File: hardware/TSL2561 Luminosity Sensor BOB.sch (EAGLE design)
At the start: 15 parts, among them U1 TSL2561FN

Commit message: Review for reds (hardware only)
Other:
- note added: "1.0"
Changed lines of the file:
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@@
 <grid distance="0.1" unitdist="inch" unit="inch" style="lines" multiple="1" display="no" altdistance="0.01" altunitdist="inch" altunit="inch"/>
 <layers>
-<layer number="1" name="Top" color="4" fill="1" visible="yes" active="no"/>
-<layer number="2" name="Route2" color="1" fill="3" visible="yes" active="no"/>
-<layer number="3" name="Route3" color="4" fill="3" visible="yes" active="no"/>
-<layer number="4" name="Route4" color="1" fill="4" visible="yes" active="no"/>
-<layer number="5" name="Route5" color="4" fill="4" visible="yes" active="no"/>
-<layer number="6" name="Route6" color="1" fill="8" visible="yes" active="no"/>
-<layer number="7" name="Route7" color="4" fill="8" visible="yes" active="no"/>
-<layer number="8" name="Route8" color="1" fill="2" visible="yes" active="no"/>
-<layer number="9" name="Route9" color="4" fill="2" visible="yes" active="no"/>
-<layer number="10" name="Route10" color="1" fill="7" visible="yes" active="no"/>
-<layer number="11" name="Route11" color="4" fill="7" visible="yes" active="no"/>
-<layer number="12" name="Route12" color="1" fill="5" visible="yes" active="no"/>
-<layer number="13" name="Route13" color="4" fill="5" visible="yes" active="no"/>
-<layer number="14" name="Route14" color="1" fill="6" visible="yes" active="no"/>
-<layer number="15" name="Route15" color="4" fill="6" visible="yes" active="no"/>
-<layer number="16" name="Bottom" color="1" fill="1" visible="yes" active="no"/>
-<layer number="17" name="Pads" color="2" fill="1" visible="yes" active="no"/>
-<layer number="18" name="Vias" color="2" fill="1" visible="yes" active="no"/>
-<layer number="19" name="Unrouted" color="6" fill="1" visible="yes" active="no"/>
-<layer number="20" name="Dimension" color="15" fill="1" visible="yes" active="no"/>
-<layer number="21" name="tPlace" color="7" fill="1" visible="yes" active="no"/>
-<layer number="22" name="bPlace" color="7" fill="1" visible="yes" active="no"/>
-<layer number="23" name="tOrigins" color="15" fill="1" visible="yes" active="no"/>
-<layer number="24" name="bOrigins" color="15" fill="1" visible="yes" active="no"/>
-<layer number="25" name="tNames" color="7" fill="1" visible="yes" active="no"/>
-<layer number="26" name="bNames" color="7" fill="1" visible="yes" active="no"/>
-<layer number="27" name="tValues" color="7" fill="1" visible="yes" active="no"/>
-<layer number="28" name="bValues" color="7" fill="1" visible="yes" active="no"/>
+<layer number="1" name="Top" color="4" fill="1" visible="no" active="no"/>
+<layer number="2" name="Route2" color="1" fill="3" visible="no" active="no"/>
+<layer number="3" name="Route3" color="4" fill="3" visible="no" active="no"/>
+<layer number="4" name="Route4" color="1" fill="4" visible="no" active="no"/>
+<layer number="5" name="Route5" color="4" fill="4" visible="no" active="no"/>
+<layer number="6" name="Route6" color="1" fill="8" visible="no" active="no"/>
+<layer number="7" name="Route7" color="4" fill="8" visible="no" active="no"/>
+<layer number="8" name="Route8" color="1" fill="2" visible="no" active="no"/>
+<layer number="9" name="Route9" color="4" fill="2" visible="no" active="no"/>
+<layer number="10" name="Route10" color="1" fill="7" visible="no" active="no"/>
+<layer number="11" name="Route11" color="4" fill="7" visible="no" active="no"/>
+<layer number="12" name="Route12" color="1" fill="5" visible="no" active="no"/>
+<layer number="13" name="Route13" color="4" fill="5" visible="no" active="no"/>
+<layer number="14" name="Route14" color="1" fill="6" visible="no" active="no"/>
+<layer number="15" name="Route15" color="4" fill="6" visible="no" active="no"/>
+<layer number="16" name="Bottom" color="1" fill="1" visible="no" active="no"/>
+<layer number="17" name="Pads" color="2" fill="1" visible="no" active="no"/>
+<layer number="18" name="Vias" color="2" fill="1" visible="no" active="no"/>
+<layer number="19" name="Unrouted" color="6" fill="1" visible="no" active="no"/>
+<layer number="20" name="Dimension" color="15" fill="1" visible="no" active="no"/>
+<layer number="21" name="tPlace" color="7" fill="1" visible="no" active="no"/>
+<layer number="22" name="bPlace" color="7" fill="1" visible="no" active="no"/>
+<layer number="23" name="tOrigins" color="15" fill="1" visible="no" active="no"/>
+<layer number="24" name="bOrigins" color="15" fill="1" visible="no" active="no"/>
+<layer number="25" name="tNames" color="7" fill="1" visible="no" active="no"/>
+<layer number="26" name="bNames" color="7" fill="1" visible="no" active="no"/>
+<layer number="27" name="tValues" color="7" fill="1" visible="no" active="no"/>
+<layer number="28" name="bValues" color="7" fill="1" visible="no" active="no"/>
 <layer number="29" name="tStop" color="7" fill="3" visible="no" active="no"/>
 <layer number="30" name="bStop" color="7" fill="6" visible="no" active="no"/>
@@
 <layer number="35" name="tGlue" color="7" fill="4" visible="no" active="no"/>
 <layer number="36" name="bGlue" color="7" fill="5" visible="no" active="no"/>
-<layer number="37" name="tTest" color="7" fill="1" visible="yes" active="no"/>
-<layer number="38" name="bTest" color="7" fill="1" visible="yes" active="no"/>
+<layer number="37" name="tTest" color="7" fill="1" visible="no" active="no"/>
+<layer number="38" name="bTest" color="7" fill="1" visible="no" active="no"/>
 <layer number="39" name="tKeepout" color="4" fill="11" visible="no" active="no"/>
 <layer number="40" name="bKeepout" color="1" fill="11" visible="no" active="no"/>
@@
 <layer number="44" name="Drills" color="7" fill="1" visible="no" active="no"/>
 <layer number="45" name="Holes" color="7" fill="1" visible="no" active="no"/>
-<layer number="46" name="Milling" color="3" fill="1" visible="yes" active="no"/>
-<layer number="47" name="Measures" color="7" fill="1" visible="yes" active="no"/>
-<layer number="48" name="Document" color="7" fill="1" visible="yes" active="no"/>
-<layer number="49" name="Reference" color="7" fill="1" visible="yes" active="no"/>
-<layer number="50" name="dxf" color="7" fill="1" visible="yes" active="no"/>
-<layer number="51" name="tDocu" color="7" fill="1" visible="yes" active="no"/>
-<layer number="52" name="bDocu" color="7" fill="1" visible="yes" active="no"/>
-<layer number="53" name="tGND_GNDA" color="7" fill="9" visible="yes" active="no"/>
-<layer number="54" name="bGND_GNDA" color="1" fill="9" visible="yes" active="no"/>
-<layer number="56" name="wert" color="7" fill="1" visible="yes" active="no"/>
+<layer number="46" name="Milling" color="3" fill="1" visible="no" active="no"/>
+<layer number="47" name="Measures" color="7" fill="1" visible="no" active="no"/>
+<layer number="48" name="Document" color="7" fill="1" visible="no" active="no"/>
+<layer number="49" name="Reference" color="7" fill="1" visible="no" active="no"/>
+<layer number="50" name="dxf" color="7" fill="1" visible="no" active="no"/>
+<layer number="51" name="tDocu" color="7" fill="1" visible="no" active="no"/>
+<layer number="52" name="bDocu" color="7" fill="1" visible="no" active="no"/>
+<layer number="53" name="tGND_GNDA" color="7" fill="9" visible="no" active="no"/>
+<layer number="54" name="bGND_GNDA" color="1" fill="9" visible="no" active="no"/>
+<layer number="56" name="wert" color="7" fill="1" visible="no" active="no"/>
 <layer number="91" name="Nets" color="2" fill="1" visible="yes" active="yes"/>
 <layer number="92" name="Busses" color="1" fill="1" visible="yes" active="yes"/>
@@
 <text x="48.26" y="132.08" size="1.778" layer="97">OPEN BOTH SIDES OF SJ1
 TO DISABLE I2C PULLUPS</text>
+<text x="239.268" y="6.604" size="2.54" layer="94" ratio="15">1.0</text>
 </plain>
 <instances>

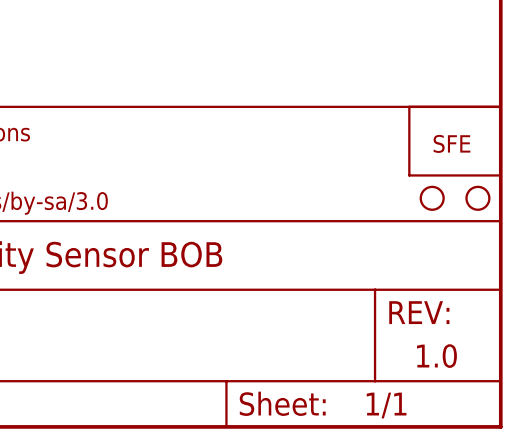
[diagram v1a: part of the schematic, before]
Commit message: Hardware version 1.0
added micro-fiducials
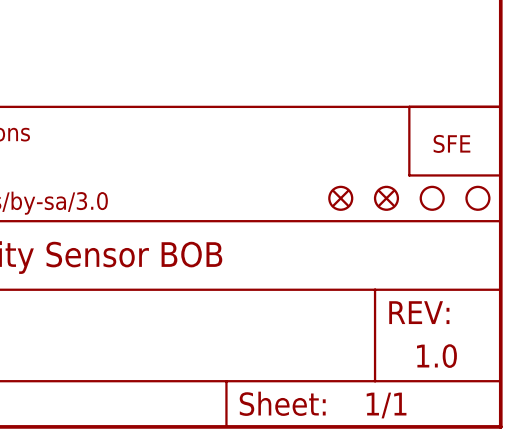
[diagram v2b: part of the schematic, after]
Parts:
- added FID1, FID2: FIDUCIALUFIDUCIAL, SparkFun-Aesthetics:FIDUCIALUFIDUCIAL
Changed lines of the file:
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@@
 <part name="R4" library="SparkFun-Resistors" deviceset="RESISTOR" device="0603" value="10K"/>
 <part name="SUPPLY5" library="SparkFun-Aesthetics" deviceset="VCC" device="" value="3.3V"/>
+<part name="FID1" library="SparkFun-Aesthetics" deviceset="FIDUCIAL" device="UFIDUCIAL"/>
+<part name="FID2" library="SparkFun-Aesthetics" deviceset="FIDUCIAL" device="UFIDUCIAL"/>
 </parts>
 <sheets>
@@
 <text x="48.26" y="132.08" size="1.778" layer="97">OPEN BOTH SIDES OF SJ1
 TO DISABLE I2C PULLUPS</text>
-<text x="239.268" y="6.604" size="2.54" layer="94" ratio="15">1.0</text>
+<text x="239.268" y="6.604" size="2.54" layer="94" ratio="10">1.0</text>
 </plain>
 <instances>
@@
 <instance part="R4" gate="G$1" x="114.3" y="124.46" rot="R90"/>
 <instance part="SUPPLY5" gate="1" x="114.3" y="142.24"/>
+<instance part="FID1" gate="G$1" x="236.22" y="25.4"/>
+<instance part="FID2" gate="G$1" x="231.14" y="25.4"/>
 </instances>
 <busses>

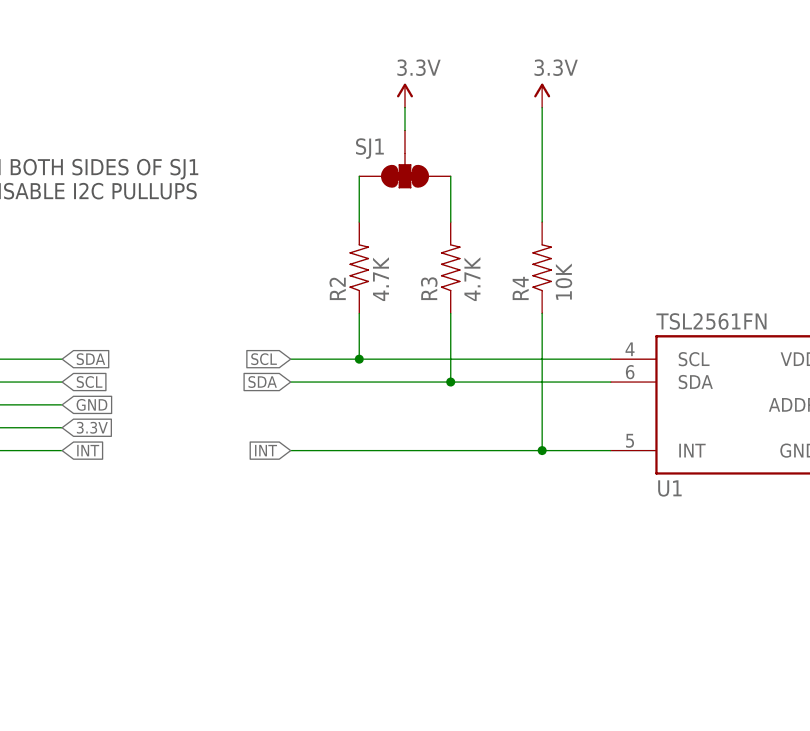
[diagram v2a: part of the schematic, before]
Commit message: Updating BRD/SCH files to current lib parts
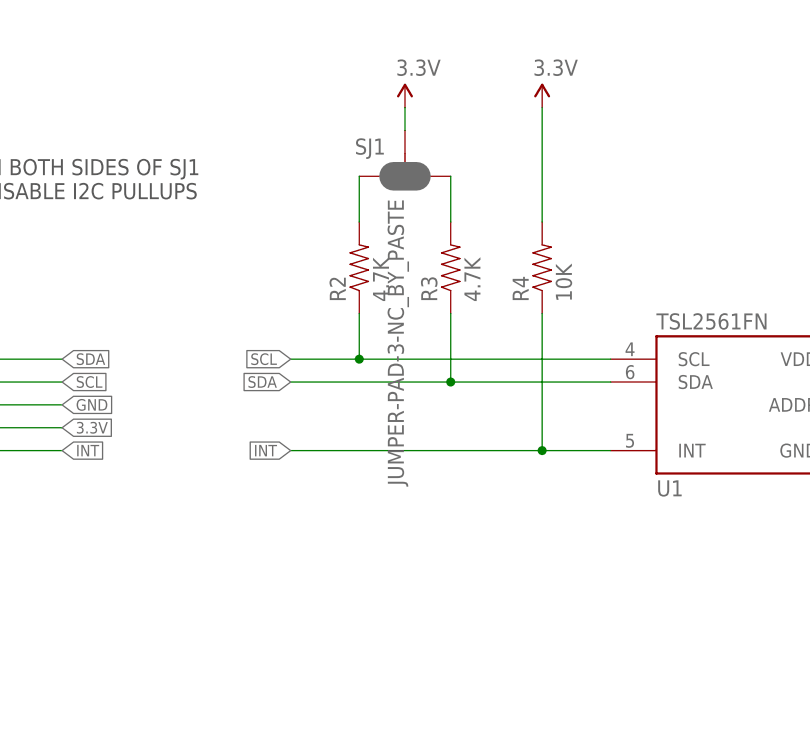
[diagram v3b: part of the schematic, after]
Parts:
- C1: device SparkFun-Capacitors:CAP0603-CAP -> SparkFun-Capacitors:0.1UF-25V(+80/-20%)(0603)
- JP1: device mike-temp:M05_ROUNDONLY_NOSILK -> SparkFun-Connectors:M05NO_SILK
- R1, R4: device SparkFun-Resistors:RESISTOR0603 -> SparkFun-Resistors:10KOHM-1/10W-1%(0603)0603
- R2, R3: device SparkFun-Resistors:RESISTOR0603 -> SparkFun-Resistors:4.7KOHM-1/10W-1%(0603)
- SJ1: value (none) -> JUMPER-PAD-3-NC_BY_PASTE; device mike-temp:SOLDERJUMPER_2WAYPASTE1&2&3 -> SparkFun-Passives:JUMPER-PAD-3-NC_BY_PASTE
- U1: device mike-temp:TSL2561FN -> SparkFun-DigitalIC:TSL2561FN
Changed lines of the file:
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@@
 <?xml version="1.0" encoding="utf-8"?>
 <!DOCTYPE eagle SYSTEM "eagle.dtd">
-<eagle version="6.4">
+<eagle version="7.2.0">
 <drawing>
 <settings>
@@
 <layer number="54" name="bGND_GNDA" color="1" fill="9" visible="no" active="no"/>
 <layer number="56" name="wert" color="7" fill="1" visible="no" active="no"/>
+<layer number="57" name="tCAD" color="7" fill="1" visible="no" active="no"/>
+<layer number="59" name="tCarbon" color="7" fill="1" visible="no" active="no"/>
+<layer number="60" name="bCarbon" color="7" fill="1" visible="no" active="no"/>
+<layer number="90" name="Modules" color="5" fill="1" visible="yes" active="yes"/>
 <layer number="91" name="Nets" color="2" fill="1" visible="yes" active="yes"/>
 <layer number="92" name="Busses" color="1" fill="1" visible="yes" active="yes"/>
@@
 <layer number="97" name="Info" color="7" fill="1" visible="yes" active="yes"/>
 <layer number="98" name="Guide" color="6" fill="1" visible="yes" active="yes"/>
+<layer number="99" name="SpiceOrder" color="7" fill="1" visible="yes" active="yes"/>
 <layer number="100" name="Muster" color="7" fill="1" visible="no" active="no"/>
 <layer number="101" name="Patch_Top" color="12" fill="4" visible="no" active="yes"/>
@@
 <layer number="108" name="tplace-old" color="10" fill="1" visible="yes" active="yes"/>
 <layer number="109" name="ref-old" color="11" fill="1" visible="yes" active="yes"/>
+<layer number="110" name="fp0" color="7" fill="1" visible="yes" active="yes"/>
+<layer number="111" name="LPC17xx" color="7" fill="1" visible="yes" active="yes"/>
+<layer number="112" name="tSilk" color="7" fill="1" visible="yes" active="yes"/>
+<layer number="113" name="IDFDebug" color="7" fill="1" visible="yes" active="yes"/>
 <layer number="116" name="Patch_BOT" color="9" fill="4" visible="no" active="yes"/>
 <layer number="121" name="_tsilk" color="7" fill="1" visible="no" active="yes"/>
 <layer number="122" name="_bsilk" color="7" fill="1" visible="no" active="yes"/>
+<layer number="123" name="tTestmark" color="7" fill="1" visible="yes" active="yes"/>
+<layer number="124" name="bTestmark" color="7" fill="1" visible="yes" active="yes"/>
 <layer number="125" name="_tNames" color="7" fill="1" visible="no" active="yes"/>
+<layer number="126" name="_bNames" color="7" fill="1" visible="yes" active="yes"/>
+<layer number="127" name="_tValues" color="7" fill="1" visible="yes" active="yes"/>
+<layer number="128" name="_bValues" color="7" fill="1" visible="yes" active="yes"/>
+<layer number="129" name="Mask" color="7" fill="1" visible="yes" active="yes"/>
+<layer number="131" name="tAdjust" color="7" fill="1" visible="yes" active="yes"/>
+<layer number="132" name="bAdjust" color="7" fill="1" visible="yes" active="yes"/>
 <layer number="144" name="Drill_legend" color="7" fill="1" visible="no" active="yes"/>
+<layer number="150" name="Notes" color="7" fill="1" visible="yes" active="yes"/>
 <layer number="151" name="HeatSink" color="7" fill="1" visible="no" active="yes"/>
+<layer number="152" name="_bDocu" color="7" fill="1" visible="yes" active="yes"/>
+<layer number="153" name="FabDoc1" color="7" fill="1" visible="yes" active="yes"/>
+<layer number="154" name="FabDoc2" color="7" fill="1" visible="yes" active="yes"/>
+<layer number="155" name="FabDoc3" color="7" fill="1" visible="yes" active="yes"/>
 <layer number="199" name="Contour" color="7" fill="1" visible="no" active="yes"/>
 <layer number="200" name="200bmp" color="1" fill="10" visible="no" active="yes"/>
@@
 <layer number="223" name="223bmp" color="24" fill="1" visible="no" active="no"/>
 <layer number="224" name="224bmp" color="25" fill="1" visible="no" active="no"/>
+<layer number="225" name="225bmp" color="7" fill="1" visible="yes" active="yes"/>
+<layer number="226" name="226bmp" color="7" fill="1" visible="yes" active="yes"/>
+<layer number="227" name="227bmp" color="7" fill="1" visible="yes" active="yes"/>
+<layer number="228" name="228bmp" color="7" fill="1" visible="yes" active="yes"/>
+<layer number="229" name="229bmp" color="7" fill="1" visible="yes" active="yes"/>
+<layer number="230" name="230bmp" color="7" fill="1" visible="yes" active="yes"/>
+<layer number="231" name="231bmp" color="7" fill="1" visible="yes" active="yes"/>
+<layer number="248" name="Housing" color="7" fill="1" visible="yes" active="yes"/>
+<layer number="249" name="Edge" color="7" fill="1" visible="yes" active="yes"/>
 <layer number="250" name="Descript" color="3" fill="1" visible="no" active="no"/>
 <layer number="251" name="SMDround" color="12" fill="11" visible="no" active="no"/>
 <layer number="254" name="cooling" color="7" fill="1" visible="no" active="yes"/>
+<layer number="255" name="routoute" color="7" fill="1" visible="yes" active="yes"/>
 </layers>
 <schematic xreflabel="%F%N/%S.%C%R" xrefpart="/%S.%C%R">
@@
 <parts>
 <part name="FRAME1" library="SparkFun-Aesthetics" deviceset="FRAME-LETTER" device=""/>
-<part name="U1" library="mike-temp" deviceset="TSL2561" device="FN" value="TSL2561FN"/>
-<part name="SJ1" library="mike-temp" deviceset="SOLDERJUMPER_2WAY" device="PASTE1&amp;2&amp;3"/>
+<part name="U1" library="SparkFun-DigitalIC" deviceset="TSL2561" device="FN" value="TSL2561FN"/>
+<part name="SJ1" library="SparkFun-Passives" deviceset="JUMPER-PAD-3-NC_BY_PASTE" device=""/>
 <part name="SJ2" library="mike-temp" deviceset="SOLDERJUMPER_2WAY" device="S"/>
-<part name="R1" library="SparkFun-Resistors" deviceset="RESISTOR" device="0603" value="10K"/>
-<part name="R2" library="SparkFun-Resistors" deviceset="RESISTOR" device="0603" value="4.7K"/>
-<part name="R3" library="SparkFun-Resistors" deviceset="RESISTOR" device="0603" value="4.7K"/>
-<part name="C1" library="SparkFun-Capacitors" deviceset="CAP" device="0603-CAP" value="0.1uF"/>
+<part name="R1" library="SparkFun-Resistors" deviceset="10KOHM-1/10W-1%(0603)" device="0603" value="10K"/>
+<part name="R2" library="SparkFun-Resistors" deviceset="4.7KOHM-1/10W-1%(0603)" device="" value="4.7K"/>
+<part name="R3" library="SparkFun-Resistors" deviceset="4.7KOHM-1/10W-1%(0603)" device="" value="4.7K"/>
+<part name="C1" library="SparkFun-Capacitors" deviceset="0.1UF-25V(+80/-20%)(0603)" device="" value="0.1uF"/>
 <part name="SUPPLY1" library="SparkFun-Aesthetics" deviceset="VCC" device="" value="3.3V"/>
 <part name="SUPPLY2" library="SparkFun-Aesthetics" deviceset="VCC" device="" value="3.3V"/>
@@
 <part name="GND2" library="SparkFun-Aesthetics" deviceset="GND" device=""/>
 <part name="GND3" library="SparkFun-Aesthetics" deviceset="GND" device=""/>
-<part name="JP1" library="mike-temp" deviceset="M05" device="_ROUNDONLY_NOSILK"/>
+<part name="JP1" library="SparkFun-Connectors" deviceset="M05" device="NO_SILK"/>
 <part name="LOGO1" library="SparkFun-Aesthetics" deviceset="OSHW-LOGO" device="S"/>
 <part name="LOGO2" library="SparkFun-Aesthetics" deviceset="LOGO-SFE" device="NW2" value="LOGO-SFENW2"/>
@@
 <part name="STANDOFF2" library="SparkFun-Electromechanical" deviceset="STAND-OFF" device=""/>
 <part name="LOGO3" library="SparkFun-Aesthetics" deviceset="SFE_LOGO_FLAME" device=".1_INCH" value="SFE_LOGO_FLAME.1_INCH"/>
-<part name="R4" library="SparkFun-Resistors" deviceset="RESISTOR" device="0603" value="10K"/>
+<part name="R4" library="SparkFun-Resistors" deviceset="10KOHM-1/10W-1%(0603)" device="0603" value="10K"/>
 <part name="SUPPLY5" library="SparkFun-Aesthetics" deviceset="VCC" device="" value="3.3V"/>
 <part name="FID1" library="SparkFun-Aesthetics" deviceset="FIDUCIAL" device="UFIDUCIAL"/>
